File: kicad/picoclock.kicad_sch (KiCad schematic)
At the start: 14 parts, among them SW1 Reset, SW2 Cycle, SW3 Shift, SW4 Set, SW5 Start/Stop, SW6 Pulse, U1 Pico

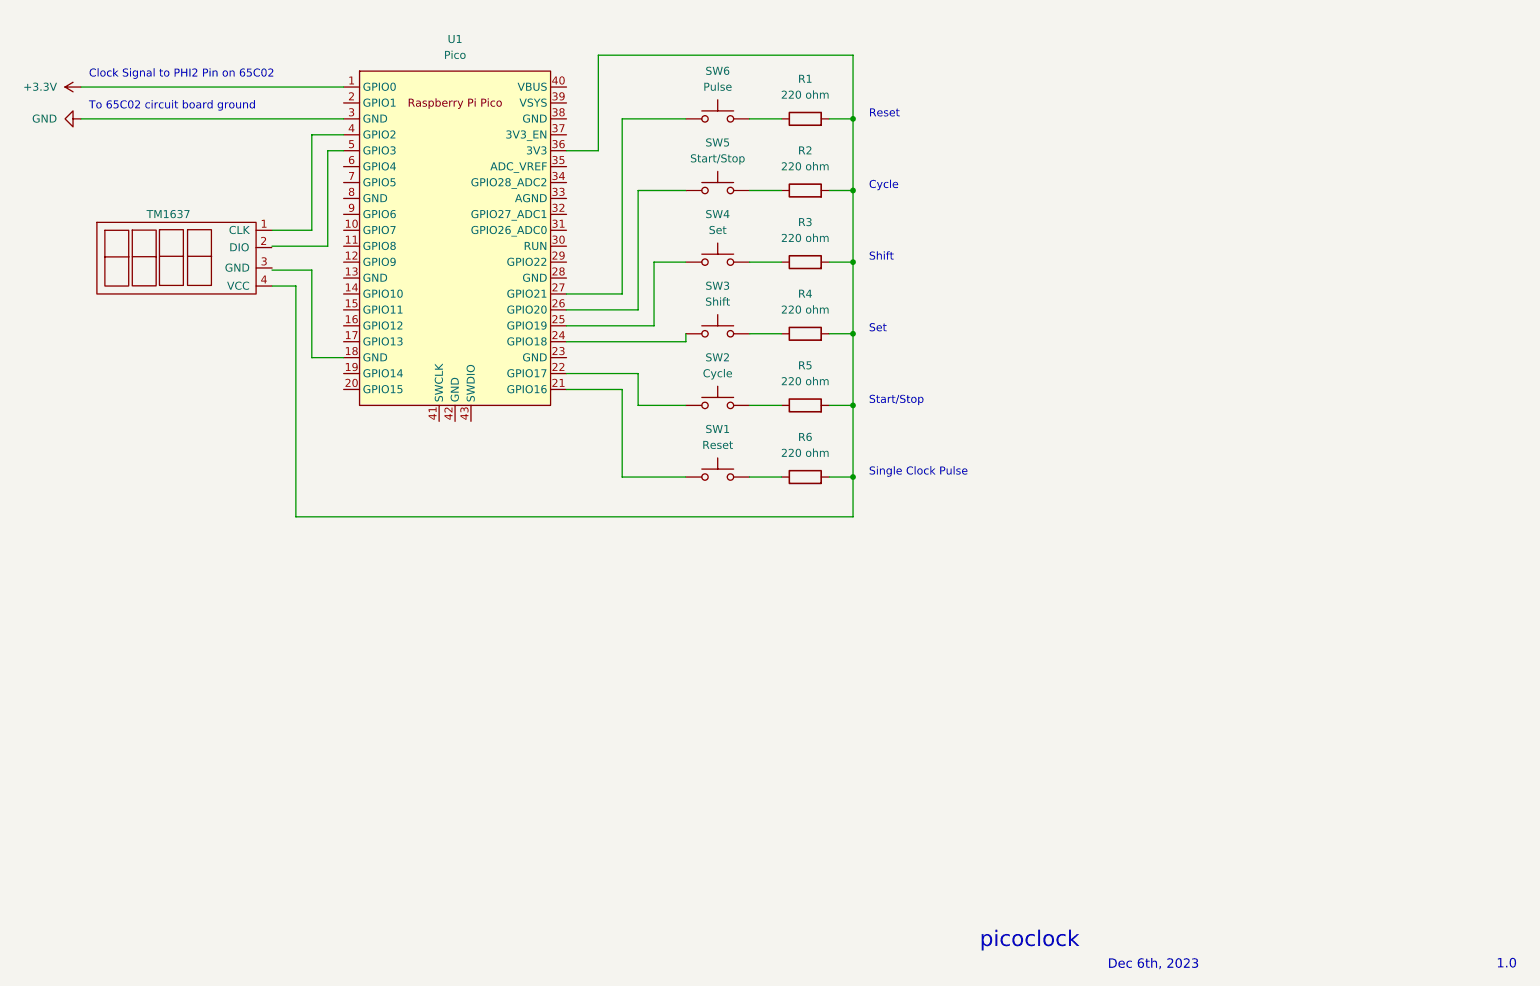
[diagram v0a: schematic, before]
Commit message: updated with protoboard layout, code updates for rotary encoder, and changed schematic
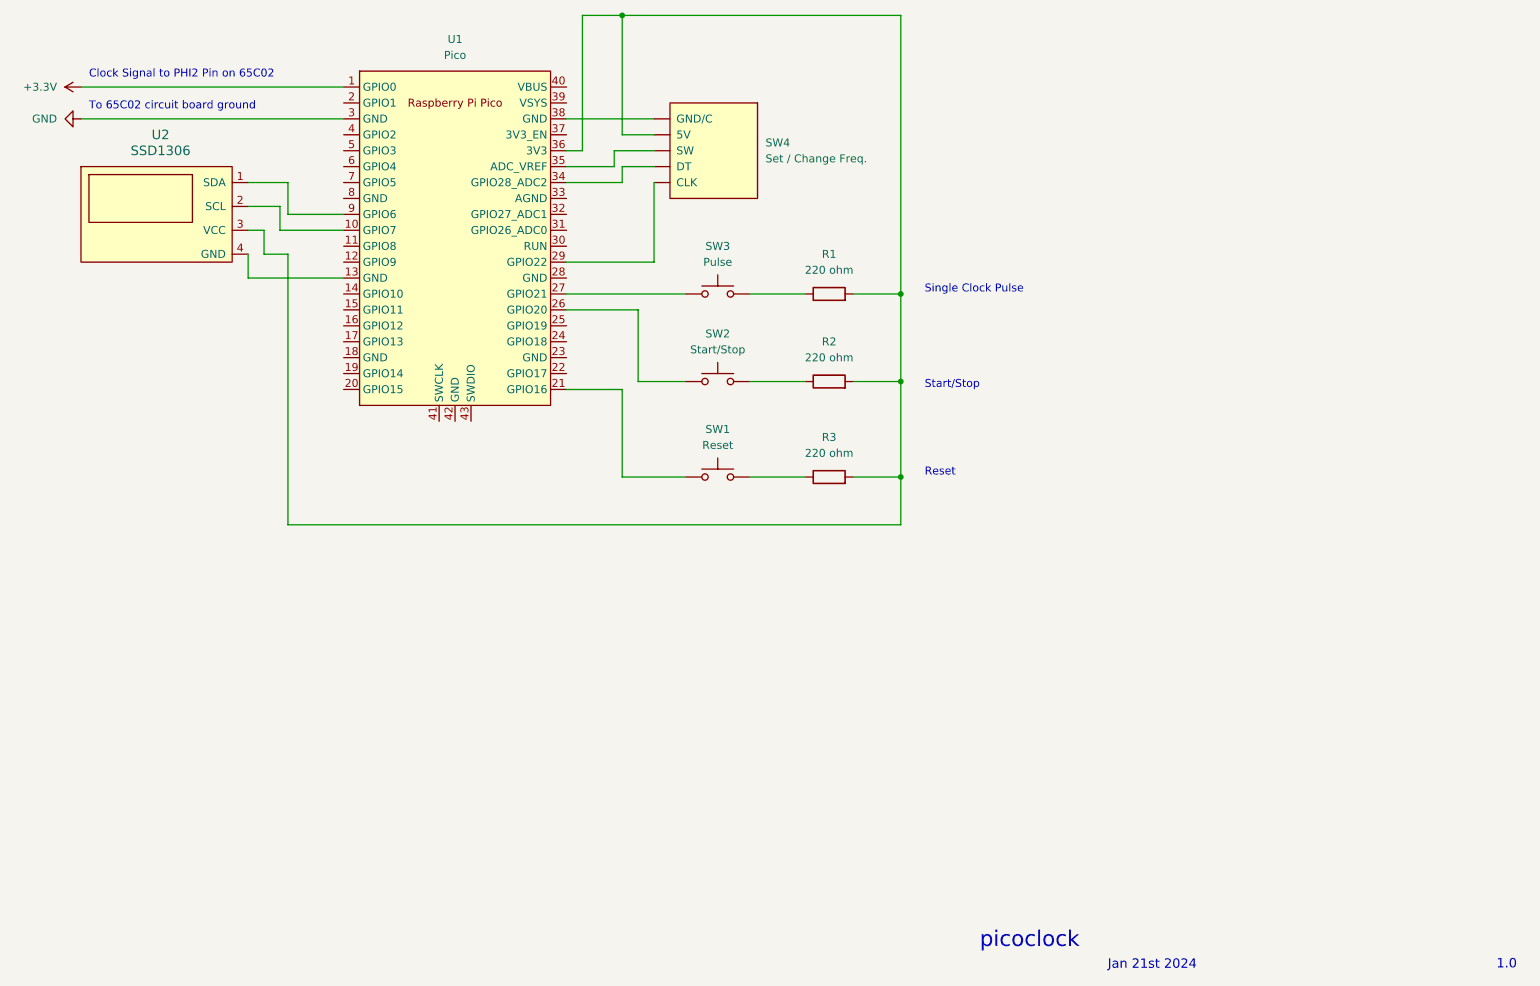
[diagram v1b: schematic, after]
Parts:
- removed R2, R3, R4: 220 ohm, symbol Device:R
- removed SW3: Shift, symbol Switch:SW_Push
- removed SW4: Set, symbol Switch:SW_Push
- removed SW5: Start/Stop, symbol Switch:SW_Push
- removed TM1637: LOGO, symbol TM1637 i2c:LOGO
- added SW4: Set / Change Freq., symbol rotary enc:KY-040
- added U2: SSD1306, symbol ssd1306:SSD1306
- SW2: value Cycle -> Start/Stop
- renumbered R5 to R2, R6 to R3, SW6 to SW3
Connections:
- net at U1.26 (GPIO20): now also SW2.1
- net at R1.2, R2.2, R3.2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: now also SW4.~ (SW), U2.3 (VCC)
- net at U1.22 (GPIO17): no longer SW2.1
- net at U1.10 (GPIO7): now also U2.2 (SCL)
- net at U1.13 (GND): now also U2.4 (GND)
- net at U1.29 (GPIO22): now also SW4.~ (SW)
- net at U1.34 (GPIO28_ADC2): now also SW4.~ (SW)
- net at U1.35 (ADC_VREF): now also SW4.~ (SW)
- net at U1.38 (GND): now also SW4.~ (SW)
- net at U1.9 (GPIO6): now also U2.1 (SDA)
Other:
- note added: "Jan 21st 2024"
- note removed: "Cycle"
- note removed: "Dec 6th, 2023"
- note removed: "Set"
- note removed: "Shift"
- moved on the sheet: R1, R2, R3, SW2, SW3

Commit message: Updated schematic and layout, changes to code to move pins about
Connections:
- net at SW4.~ (SW): now also U1.38 (GND); no longer U1.35 (ADC_VREF)
- net at U1.22 (GPIO17): now also SW4.~ (SW)
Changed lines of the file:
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@@
+    (stroke (width 0) (type default))
+  )
+  (wire (pts (xy 120.65 99.06) (xy 127 99.06))
     (stroke (width 0) (type default))
   )
@@
     (stroke (width 0) (type default))
   )
-  (wire (pts (xy 128.27 63.5) (xy 128.27 66.04))
+  (wire (pts (xy 127 63.5) (xy 127 99.06))
     (stroke (width 0) (type default))
   )
@@
   )
   (wire (pts (xy 43.18 58.42) (xy 85.09 58.42))
-    (stroke (width 0) (type default))
-  )
-  (wire (pts (xy 128.27 66.04) (xy 120.65 66.04))
     (stroke (width 0) (type default))
   )
@@
     (stroke (width 0) (type default))
   )
-  (wire (pts (xy 134.62 63.5) (xy 128.27 63.5))
+  (wire (pts (xy 134.62 63.5) (xy 127 63.5))
     (stroke (width 0) (type default))
   )
